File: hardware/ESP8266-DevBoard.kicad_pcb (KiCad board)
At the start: 2 copper layers, 61 x 40.6 mm, 28 parts, among them J1 Conn_01x08, J2 Conn_01x08, P1 USB_C_Plug_USB2.0, Q1 BSS138, Q2 BSS138, SW1 SW_Push, SW2 SW_Push, U1 AMS1117-3.3, U2 CH340C, U3 ESP-12F

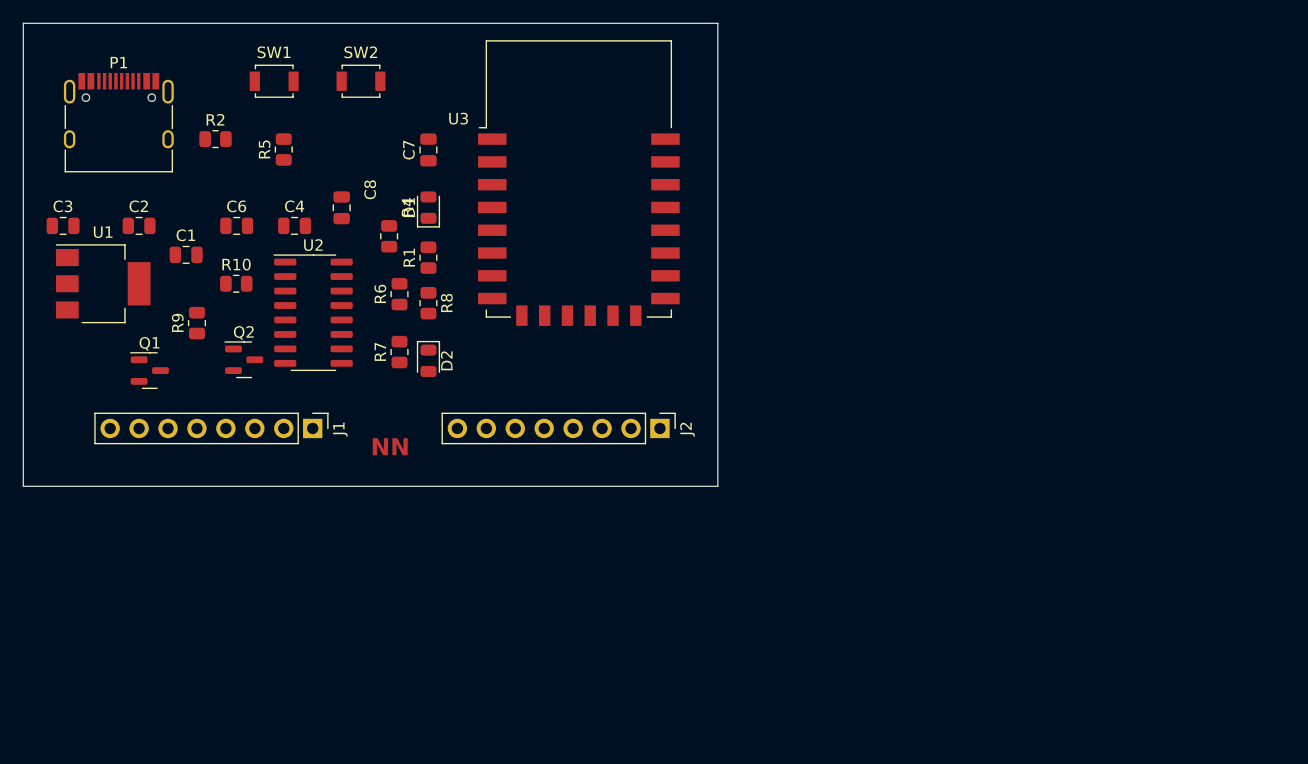
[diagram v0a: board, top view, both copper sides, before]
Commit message: Complete PCB routing and layout
- Routed all power traces (5V, 3.3V, GND)
- Routed all signal connections (USB, UART, GPIO)
- Component placement optimized for routing
- PCB ready for design rule check and manufacturing
- 2-layer board design
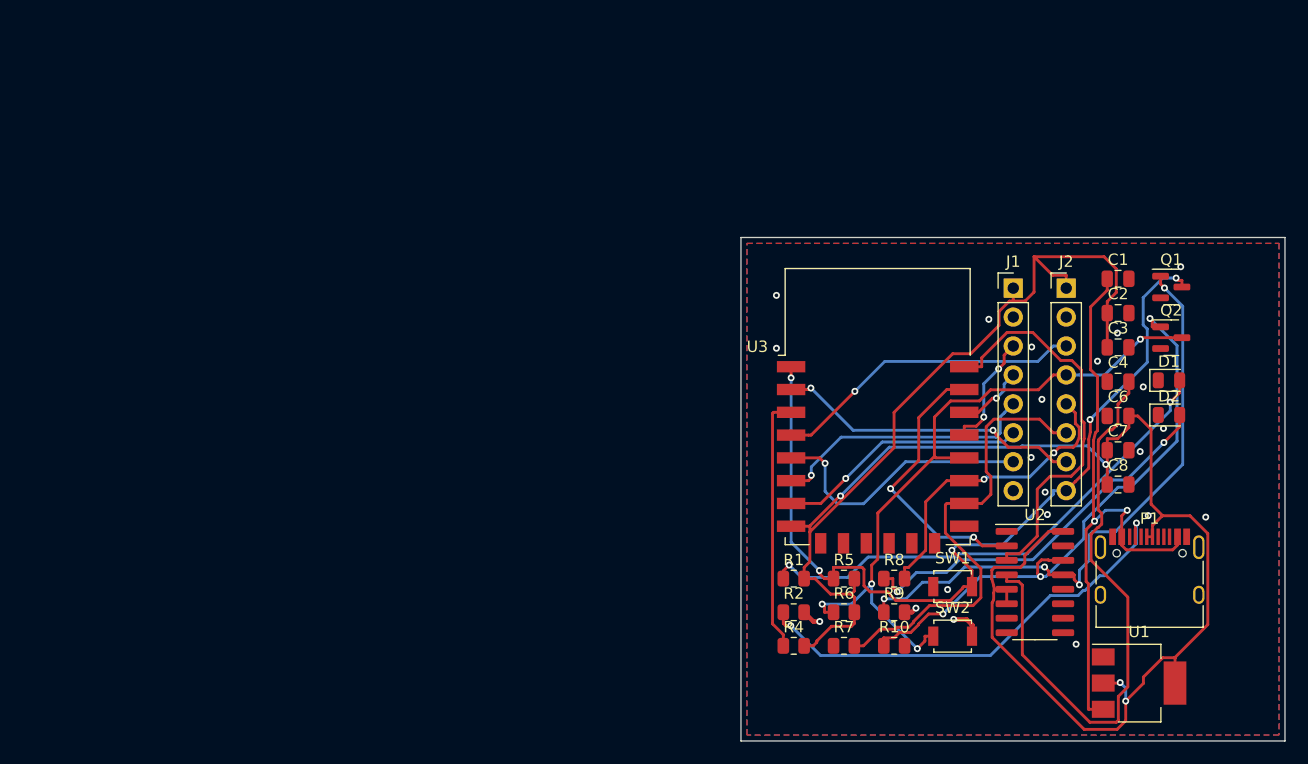
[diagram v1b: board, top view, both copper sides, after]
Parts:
- moved P1 98.9 mm to (131.9, 82.1)
- moved U1 97.5 mm to (131.0, 90.9)
- moved C3 93.2 mm to (129.1, 61.5)
- moved Q1 90.0 mm to (133.8, 56.2)
- moved C2 86.3 mm to (129.1, 58.5)
- moved C1 81.8 mm to (129.1, 55.4)
- moved Q2 81.4 mm to (133.8, 60.6)
- moved C6 79.1 mm to (129.1, 67.5)
- moved SW1 74.3 mm to (114.6, 82.5)
- moved C4 73.6 mm to (129.1, 64.5)
- moved C8 72.4 mm to (129.1, 73.5), turned to 0 degrees
- moved SW2 71.2 mm to (114.6, 86.8)
- moved U2 67.6 mm to (121.8, 82.1)
- moved D1 66.7 mm to (133.6, 64.4), turned to 0 degrees
- moved R9 66.3 mm to (109.5, 84.7), turned to 0 degrees
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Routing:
- net +3.3V: track 0.00 -> 187.5 mm, vias 0 -> 4
- net /RST: track 0.00 -> 77.5 mm, vias 0 -> 5
- net /GPIO0(D3): track 0.00 -> 60.3 mm, vias 0 -> 4
- net Net-(Q1-G): track 0.00 -> 53.4 mm, vias 0 -> 4
- net +5V: track 0.00 -> 53.0 mm, vias 0 -> 2
- net Net-(U2-V3): track 0.00 -> 52.4 mm
- net Net-(Q2-G): track 0.00 -> 51.4 mm, vias 0 -> 3
- net Net-(D1-A): track 0.00 -> 44.4 mm, vias 0 -> 2
- net /GPIO15(D8): track 0.00 -> 40.6 mm
- net Net-(P1-CC): track 0.00 -> 40.3 mm, vias 0 -> 2
- net Net-(U2-RXD): track 0.00 -> 34.7 mm
- net Net-(D2-A): track 0.00 -> 33.9 mm, vias 0 -> 2
- net /GPIO16(D0): track 0.00 -> 27.4 mm, vias 0 -> 1
- net /GPIO2(D4): track 0.00 -> 27.1 mm, vias 0 -> 2
- net /ADC0(A0): track 0.00 -> 27.0 mm, vias 0 -> 2
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- added copper zone on B.Cu, net GND
- added copper zone on F.Cu, net GND
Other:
- board size 61 x 40.6 mm -> 47.8 x 44.2 mm
- board text removed: "NN"
